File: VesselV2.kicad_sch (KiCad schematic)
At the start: 205 parts, among them U1 ATmega32U4-A

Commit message: Late night PCB organization (WIP)
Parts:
- added S1, S2, S3: MX_stab, PCM_marbastlib-mx:STAB_MX_P_2u, symbol PCM_marbastlib-mx:MX_stab
- added S4: MX_stab, PCM_marbastlib-mx:STAB_MX_P_6.25u, symbol PCM_marbastlib-mx:MX_stab
- MX45, MX61, MX91: footprint PCM_marbastlib-mx:STAB_MX_2u -> PCM_marbastlib-mx:SW_MX_1u
- MX97: footprint PCM_marbastlib-mx:STAB_MX_6.25u -> PCM_marbastlib-mx:SW_MX_1u
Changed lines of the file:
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@@
       (effects (font (size 1.27 1.27)))
     )
-    (property "Footprint" "PCM_marbastlib-mx:STAB_MX_6.25u" (at 196.85 162.56 0)
+    (property "Footprint" "PCM_marbastlib-mx:SW_MX_1u" (at 196.85 162.56 0)
       (effects (font (size 1.27 1.27)) hide)
     )
@@
     )
   )
+  (symbol (lib_id "PCM_marbastlib-mx:MX_stab") (at 194.31 203.2 0) (unit 1)
+    (in_bom yes) (on_board yes) (dnp no) (fields_autoplaced)
+    (property "Reference" "S4" (at 200.66 201.803 0)
+      (effects (font (size 1.27 1.27)) (justify left))
+    )
+    (property "Value" "MX_stab" (at 200.66 204.343 0)
+      (effects (font (size 1.27 1.27)) (justify left))
+    )
+    (property "Footprint" "PCM_marbastlib-mx:STAB_MX_P_6.25u" (at 194.31 203.2 0)
+      (effects (font (size 1.27 1.27)) hide)
+    )
+    (property "Datasheet" "" (at 194.31 203.2 0)
+      (effects (font (size 1.27 1.27)) hide)
+    )
+    (instances
+      (project "VesselV2"
+        (path "/c445c6d8-4fde-4143-815a-ac483f9e4cc3"
+          (reference "S4") (unit 1)
+        )
+      )
+    )
+  )
   (symbol (lib_id "PCM_marbastlib-mx:MX_SW_solder") (at 231.14 146.05 0) (unit 1)
     (in_bom yes) (on_board yes) (dnp no) (fields_autoplaced)
@@
       (effects (font (size 1.27 1.27)))
     )
-    (property "Footprint" "PCM_marbastlib-mx:STAB_MX_2u" (at 265.43 146.05 0)
+    (property "Footprint" "PCM_marbastlib-mx:SW_MX_1u" (at 265.43 146.05 0)
       (effects (font (size 1.27 1.27)) hide)
     )
@@
       (effects (font (size 1.27 1.27)))
     )
-    (property "Footprint" "PCM_marbastlib-mx:STAB_MX_2u" (at 276.86 111.76 0)
+    (property "Footprint" "PCM_marbastlib-mx:SW_MX_1u" (at 276.86 111.76 0)
       (effects (font (size 1.27 1.27)) hide)
     )
@@
     )
   )
+  (symbol (lib_id "PCM_marbastlib-mx:MX_stab") (at 311.15 177.8 0) (unit 1)
+    (in_bom yes) (on_board yes) (dnp no)
+    (property "Reference" "S1" (at 317.5 176.403 0)
+      (effects (font (size 1.27 1.27)) (justify left))
+    )
+    (property "Value" "MX_stab" (at 317.5 178.943 0)
+      (effects (font (size 1.27 1.27)) (justify left))
+    )
+    (property "Footprint" "PCM_marbastlib-mx:STAB_MX_P_2u" (at 311.15 177.8 0)
+      (effects (font (size 1.27 1.27)) hide)
+    )
+    (property "Datasheet" "" (at 311.15 177.8 0)
+      (effects (font (size 1.27 1.27)) hide)
+    )
+    (instances
+      (project "VesselV2"
+        (path "/c445c6d8-4fde-4143-815a-ac483f9e4cc3"
+          (reference "S1") (unit 1)
+        )
+      )
+    )
+  )
   (symbol (lib_id "Device:D_Small") (at 237.49 60.96 90) (unit 1)
     (in_bom yes) (on_board yes) (dnp no) (fields_autoplaced)
@@
     )
   )
+  (symbol (lib_id "PCM_marbastlib-mx:MX_stab") (at 309.88 189.23 0) (unit 1)
+    (in_bom yes) (on_board yes) (dnp no) (fields_autoplaced)
+    (property "Reference" "S2" (at 316.23 187.833 0)
+      (effects (font (size 1.27 1.27)) (justify left))
+    )
+    (property "Value" "MX_stab" (at 316.23 190.373 0)
+      (effects (font (size 1.27 1.27)) (justify left))
+    )
+    (property "Footprint" "PCM_marbastlib-mx:STAB_MX_P_2u" (at 309.88 189.23 0)
+      (effects (font (size 1.27 1.27)) hide)
+    )
+    (property "Datasheet" "" (at 309.88 189.23 0)
+      (effects (font (size 1.27 1.27)) hide)
+    )
+    (instances
+      (project "VesselV2"
+        (path "/c445c6d8-4fde-4143-815a-ac483f9e4cc3"
+          (reference "S2") (unit 1)
+        )
+      )
+    )
+  )
   (symbol (lib_id "PCM_marbastlib-mx:MX_SW_solder") (at 231.14 128.27 0) (unit 1)
     (in_bom yes) (on_board yes) (dnp no) (fields_autoplaced)
@@
       (effects (font (size 1.27 1.27)))
     )
-    (property "Footprint" "PCM_marbastlib-mx:STAB_MX_2u" (at 276.86 95.25 0)
+    (property "Footprint" "PCM_marbastlib-mx:SW_MX_1u" (at 276.86 95.25 0)
       (effects (font (size 1.27 1.27)) hide)
     )
@@
         )
       )
+    )
+  )
+  (symbol (lib_id "PCM_marbastlib-mx:MX_stab") (at 283.21 199.39 0) (unit 1)
+    (in_bom yes) (on_board yes) (dnp no) (fields_autoplaced)
+    (property "Reference" "S3" (at 289.56 197.993 0)
+      (effects (font (size 1.27 1.27)) (justify left))
+    )
+    (property "Value" "MX_stab" (at 289.56 200.533 0)
+      (effects (font (size 1.27 1.27)) (justify left))
+    )
+    (property "Footprint" "PCM_marbastlib-mx:STAB_MX_P_2u" (at 283.21 199.39 0)
+      (effects (font (size 1.27 1.27)) hide)
+    )
+    (property "Datasheet" "" (at 283.21 199.39 0)
+      (effects (font (size 1.27 1.27)) hide)
+    )
+    (instances
+      (project "VesselV2"
+        (path "/c445c6d8-4fde-4143-815a-ac483f9e4cc3"
+          (reference "S3") (unit 1)
+        )
+      )

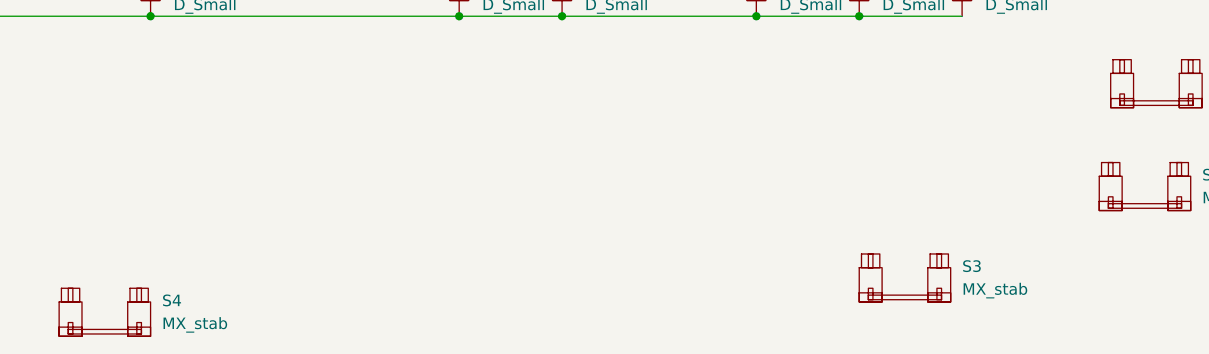
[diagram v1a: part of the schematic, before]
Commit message: Pcb build done - Adding crystal & labels
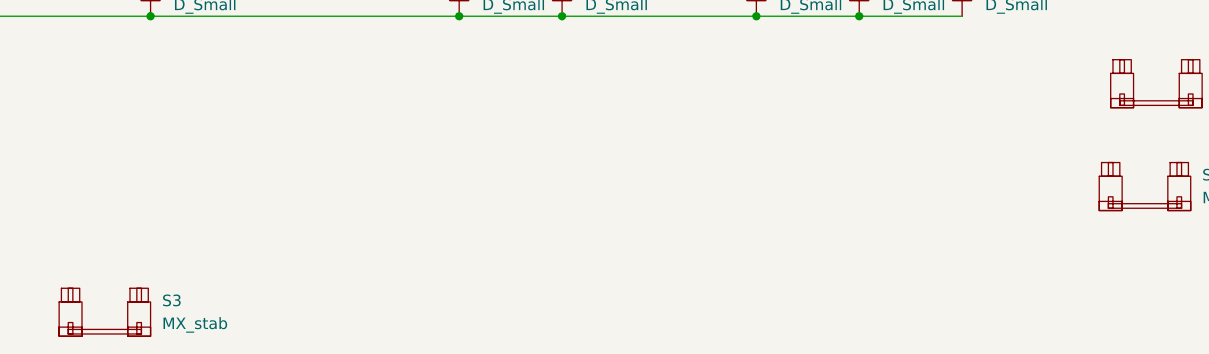
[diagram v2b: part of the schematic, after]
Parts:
- removed S3: MX_stab, PCM_marbastlib-mx:STAB_MX_P_2u, symbol PCM_marbastlib-mx:MX_stab
- MX91: footprint PCM_marbastlib-mx:SW_MX_1u -> PCM_marbastlib-mx:SW_MX_1.75u
- renumbered S4 to S3
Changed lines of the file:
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@@
   (symbol (lib_id "PCM_marbastlib-mx:MX_stab") (at 194.31 203.2 0) (unit 1)
     (in_bom yes) (on_board yes) (dnp no) (fields_autoplaced)
-    (property "Reference" "S4" (at 200.66 201.803 0)
+    (property "Reference" "S3" (at 200.66 201.803 0)
       (effects (font (size 1.27 1.27)) (justify left))
     )
@@
       (effects (font (size 1.27 1.27)) hide)
     )
+    (property "DigikeyPartNumber" "" (at 194.31 203.2 0)
+      (effects (font (size 1.27 1.27)))
+    )
     (instances
       (project "VesselV2"
         (path "/c445c6d8-4fde-4143-815a-ac483f9e4cc3"
-          (reference "S4") (unit 1)
+          (reference "S3") (unit 1)
         )
       )
@@
       (effects (font (size 1.27 1.27)))
     )
-    (property "Footprint" "PCM_marbastlib-mx:SW_MX_1u" (at 265.43 146.05 0)
+    (property "Footprint" "PCM_marbastlib-mx:SW_MX_1.75u" (at 265.43 146.05 0)
       (effects (font (size 1.27 1.27)) hide)
     )
@@
         )
       )
-    )
-  )
-  (symbol (lib_id "PCM_marbastlib-mx:MX_stab") (at 283.21 199.39 0) (unit 1)
-    (in_bom yes) (on_board yes) (dnp no) (fields_autoplaced)
-    (property "Reference" "S3" (at 289.56 197.993 0)
-      (effects (font (size 1.27 1.27)) (justify left))
-    )
-    (property "Value" "MX_stab" (at 289.56 200.533 0)
-      (effects (font (size 1.27 1.27)) (justify left))
-    )
-    (property "Footprint" "PCM_marbastlib-mx:STAB_MX_P_2u" (at 283.21 199.39 0)
-      (effects (font (size 1.27 1.27)) hide)
-    )
-    (property "Datasheet" "" (at 283.21 199.39 0)
-      (effects (font (size 1.27 1.27)) hide)
-    )
-    (instances
-      (project "VesselV2"
-        (path "/c445c6d8-4fde-4143-815a-ac483f9e4cc3"
-          (reference "S3") (unit 1)
-        )
-      )

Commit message: Footprint Assignment
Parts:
- added C1, C3: 22pF, Capacitor_SMD:C_0805_2012Metric_Pad1.18x1.45mm_HandSolder, symbol Device:C_Small
- added C2: 1uf, Capacitor_SMD:C_0805_2012Metric_Pad1.18x1.45mm_HandSolder, symbol Device:C_Small
- added F1: 500mA, Fuse:Fuse_1206_3216Metric_Pad1.42x1.75mm_HandSolder, symbol Device:Polyfuse_Small
- added J1: USB_A, Connector_USB:USB_A_Molex_67643_Horizontal, symbol Connector:USB_A
- added R2, R3: 22, Resistor_SMD:R_0805_2012Metric_Pad1.20x1.40mm_HandSolder, symbol Device:R_Small
- added R4, R5: 10k, Resistor_SMD:R_0805_2012Metric_Pad1.20x1.40mm_HandSolder, symbol Device:R_Small
- added SW1: SW_Push, symbol Switch:SW_Push
- added Y1: 16MHz, Crystal:Crystal_SMD_3225-4Pin_3.2x2.5mm_HandSoldering, symbol Device:Crystal_GND24_Small
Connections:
- net ROW6: now reaches D100.1 (K), D101.1 (K), D102.1 (K), D94.1 (K), D95.1 (K), D96.1 (K), D97.1 (K), D98.1 (K), D99.1 (K)
- net ROW6: now also U1.20 (PD2)
- net ROW2: now reaches U1.10 (PB2)
- net ROW2: now also D32.1 (K), D33.1 (K), D34.1 (K), D35.1 (K), D36.1 (K), D37.1 (K), D38.1 (K), D39.1 (K), D40.1 (K), D41.1 (K), D42.1 (K), D43.1 (K), D44.1 (K), D45.1 (K), D46.1 (K), D47.1 (K)
- net ROW3: now reaches U1.11 (PB3)
- net ROW3: now also D48.1 (K), D49.1 (K), D50.1 (K), D51.1 (K), D52.1 (K), D53.1 (K), D54.1 (K), D55.1 (K), D56.1 (K), D57.1 (K), D58.1 (K), D59.1 (K), D60.1 (K), D61.1 (K), D62.1 (K), D63.1 (K)
- net COL0: now reaches U1.12 (PB7)
- net COL0: now also MX1.1, MX16.1, MX32.1, MX48.1, MX64.1, MX79.1, MX94.1
- net at U1.13 (~{RESET}): now also R4.1, SW1.2
- net +5V: now reaches U1.14 (VCC), U1.34 (VCC)
- net +5V: now also U1.2 (UVCC), U1.24 (AVCC), U1.44 (AVCC), U1.7 (VBUS), F1.2, R4.2
- net GND: now reaches U1.15 (GND), U1.23 (GND), U1.35 (GND), U1.43 (GND)
- net GND: now also U1.5 (UGND), C1.1, C2.2, C3.1, J1.4 (GND), R5.2, SW1.1, Y1.2, Y1.4
- net at U1.16 (XTAL2): now also C3.2, Y1.3
- net at U1.17 (XTAL1): now also C1.2, Y1.1
- net ROW4: now reaches U1.18 (PD0)
- net ROW4: now also D64.1 (K), D65.1 (K), D66.1 (K), D67.1 (K), D68.1 (K), D69.1 (K), D70.1 (K), D71.1 (K), D72.1 (K), D73.1 (K), D74.1 (K), D75.1 (K), D76.1 (K), D77.1 (K), D78.1 (K)
- net ROW5: now reaches U1.19 (PD1)
- net ROW5: now also D79.1 (K), D80.1 (K), D81.1 (K), D82.1 (K), D83.1 (K), D84.1 (K), D85.1 (K), D86.1 (K), D87.1 (K), D88.1 (K), D89.1 (K), D90.1 (K), D91.1 (K), D92.1 (K), D93.1 (K)
- net COL1: now reaches U1.21 (PD3)
- net COL1: now also MX2.1, MX33.1, MX49.1, MX65.1, MX80.1, MX95.1
- net COL2: now reaches U1.22 (PD5)
- net COL2: now also MX17.1, MX3.1, MX34.1, MX50.1, MX66.1, MX81.1, MX96.1
- net COL3: now reaches U1.25 (PD4)
- net COL3: now also MX18.1, MX35.1, MX4.1, MX51.1, MX67.1, MX82.1
- net COL4: now reaches U1.26 (PD6)
- net COL4: now also MX19.1, MX36.1, MX5.1, MX52.1, MX68.1, MX83.1
- net COL5: now reaches U1.27 (PD7)
- net COL5: now also MX20.1, MX37.1, MX53.1, MX6.1, MX69.1, MX84.1
- net COL6: now reaches U1.28 (PB4)
- net COL6: now also MX21.1, MX38.1, MX54.1, MX7.1, MX70.1, MX85.1, MX97.1
- net COL7: now reaches U1.29 (PB5)
- net COL7: now also MX22.1, MX39.1, MX55.1, MX71.1, MX8.1, MX86.1
- net at U1.3 (D-): now also R3.2
- net COL8: now reaches U1.30 (PB6)
- net COL8: now also MX24.1, MX41.1, MX57.1, MX73.1, MX88.1, MX98.1
- net COL9: now reaches U1.31 (PC6)
- net COL9: now also MX23.1, MX40.1, MX56.1, MX72.1, MX87.1, MX9.1
- net COL10: now reaches U1.32 (PC7)
- net COL10: now also MX10.1, MX25.1, MX42.1, MX58.1, MX74.1, MX89.1, MX99.1
- net at U1.33 (~{HWB}/PE2): now also R5.1
- net COL11: now reaches U1.36 (PF7)
- net COL11: now also MX11.1, MX26.1, MX43.1, MX59.1, MX75.1, MX90.1
- net COL12: now reaches U1.37 (PF6)
- net COL12: now also MX100.1, MX12.1, MX27.1, MX44.1, MX60.1, MX76.1, MX91.1
- net COL13: now reaches U1.38 (PF5)
- net COL13: now also MX101.1, MX28.1, MX45.1, MX61.1, MX92.1
- net COL14: now reaches U1.39 (PF4)
- net COL14: now also MX102.1, MX13.1, MX29.1
- net at U1.4 (D+): now also R2.2
- net COL15: now reaches U1.40 (PF1)
- net COL15: now also MX14.1, MX30.1, MX46.1, MX62.1, MX77.1
- net COL16: now reaches U1.41 (PF0)
- net COL16: now also MX15.1, MX31.1, MX47.1, MX63.1, MX78.1, MX93.1
- net at U1.6 (UCAP): now also C2.1
- net ROW0: now reaches U1.8 (PB0)
- net ROW0: now also D1.1 (K), D10.1 (K), D11.1 (K), D12.1 (K), D13.1 (K), D14.1 (K), D15.1 (K), D2.1 (K), D3.1 (K), D4.1 (K), D5.1 (K), D6.1 (K), D7.1 (K), D8.1 (K), D9.1 (K)
- net ROW1: now reaches U1.9 (PB1)
- net ROW1: now also D16.1 (K), D17.1 (K), D18.1 (K), D19.1 (K), D20.1 (K), D21.1 (K), D22.1 (K), D23.1 (K), D24.1 (K), D25.1 (K), D26.1 (K), D27.1 (K), D28.1 (K), D29.1 (K), D30.1 (K), D31.1 (K)
- new net D+: J1.3 (D+), R2.1
- new net D-: J1.2 (D-), R3.1
- new net VCC: F1.1, J1.1 (VBUS)
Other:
- moved on the sheet: D1, D10, D100, D101, D102, D11, D12, D13, D14, D15, D16, D17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

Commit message: Footprint Assignment & Part Number association
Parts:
- removed J1: USB_A, Connector_USB:USB_A_Molex_67643_Horizontal, symbol Connector:USB_A
- added USB1: Molex-0548190589, random-keyboard-parts:Molex-0548190589, symbol random-keyboard-parts:Molex-0548190589
- C1, C3: DigikeyPartNumber (none) -> 311-1103-6-ND
- F1: DigikeyPartNumber (none) -> 486-1675-6-ND
- R2, R3: DigikeyPartNumber (none) -> RMCF0805FT22R0DKR-ND
- R4, R5: DigikeyPartNumber (none) -> RMCF0805FT10K0DKR-ND
- SW1: footprint (none) -> random-keyboard-parts:SKQG-1155865; ManufacturerPartNumber (none) -> SKQGACE010
- U1: DigikeyPartNumber (none) -> ATMEGA32U4-AU-ND
- Y1: DigikeyPartNumber (none) -> SER4069DKR-ND
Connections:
- net D+: now also USB1.3 (D+)
- net D-: now also USB1.4 (D-)
- net GND: now also USB1.1 (GND), USB1.6 (SHIELD)
- net VCC: now also USB1.5 (VBUS)
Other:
- moved on the sheet: F1

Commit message: Edge cuts done - Datasheet info filled in - Preliminary Bom generated
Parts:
- C2: DigikeyPartNumber (none) -> 399-C0402C105K9PAC7867DKR-ND
- D1, D10, D100, D101, D102, D11, D12, D13, D14, D15, D16, D17, D18, D19, D2, D20, D21, D22, D23, D24, D25, D26, D27, D28, D29, D3, D30, D31, D32, D33, D34, D35, D36, D37, D38, D39, D4, D40, D41, D42, D43, D44, D45, D46, D47, D48, D49, D5, D50, D51, D52, D53, D54, D55, D56, D57, D58, D59, D6, D60, D61, D62, D63, D64, D65, D66, D67, D68, D69, D7, D70, D71, D72, D73, D74, D75, D76, D77, D78, D79, D8, D80, D81, D82, D83, D84, D85, D86, D87, D88, D89, D9, D90, D91, D92, D93, D94, D95, D96, D97, D98, D99: DigikeyPartNumber (none) -> 1N4148WTPMSDKR-ND; ManufacturerPartNumber (none) -> 1N4148W
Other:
- moved on the sheet: R4

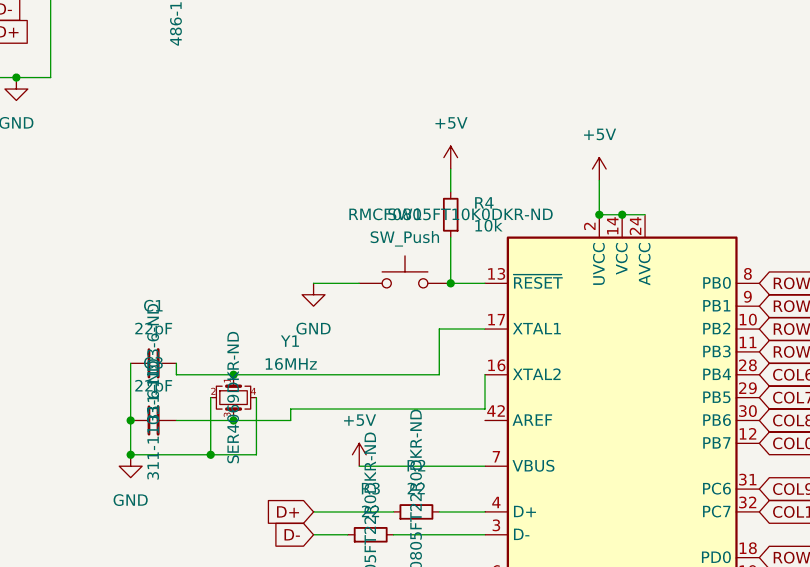
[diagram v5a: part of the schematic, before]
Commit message: Mouser partNumber fields Update - BOM Update
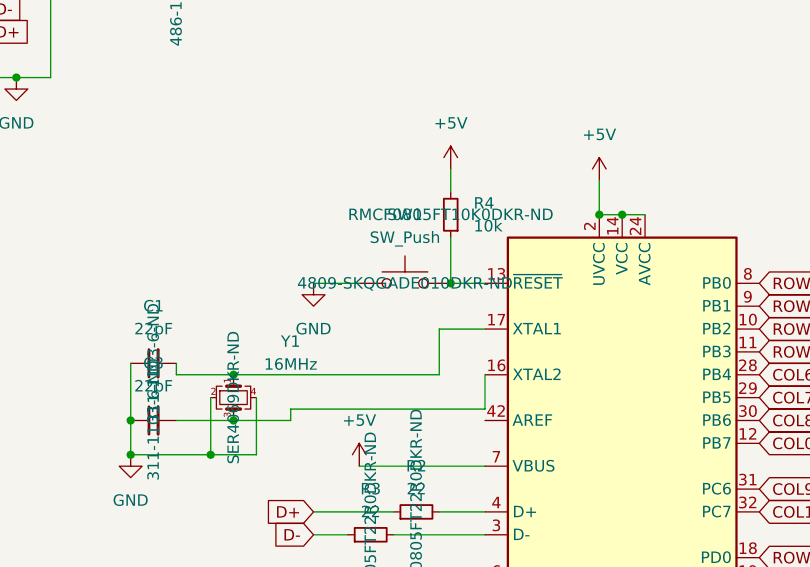
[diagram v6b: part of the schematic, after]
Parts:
- C1, C3: MouserPartNumber (none) -> 603-CC805JRNPO9BN220
- C2: MouserPartNumber (none) -> 80-C0402C105K9P
- D1, D10, D100, D101, D102, D11, D12, D13, D14, D15, D16, D17, D18, D19, D2, D20, D21, D22, D23, D24, D25, D26, D27, D28, D29, D3, D30, D31, D32, D33, D34, D35, D36, D37, D38, D39, D4, D40, D41, D42, D43, D44, D45, D46, D47, D48, D49, D5, D50, D51, D52, D53, D54, D55, D56, D57, D58, D59, D6, D60, D61, D62, D63, D64, D65, D66, D67, D68, D69, D7, D70, D71, D72, D73, D74, D75, D76, D77, D78, D79, D8, D80, D81, D82, D83, D84, D85, D86, D87, D88, D89, D9, D90, D91, D92, D93, D94, D95, D96, D97, D98, D99: MouserPartNumber (none) -> 833-1N4148W-TP
- F1: MouserPartNumber (none) -> 693-3413.0113.22
- R2, R3: MouserPartNumber (none) -> 708-RMCF0805FT22R0
- R4, R5: MouserPartNumber (none) -> 708-RMCF0805FT10K0
- SW1: DigikeyPartNumber (none) -> 4809-SKQGADE010DKR-ND; MouserPartNumber (none) -> 688-SKQGAD
- U1: MouserPartNumber (none) -> 556-ATMEGA32U4-AU
- USB1: MouserPartNumber (none) -> 538-54819-0589
- Y1: MouserPartNumber (none) -> 732-322516MF09Z-AC0

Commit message: Fixed routing errors - except USB footprint shape
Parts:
- S2: footprint PCM_marbastlib-mx:STAB_MX_P_2u -> PCM_marbastlib-mx:STAB_MX_P_ISO
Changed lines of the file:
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@@
       (effects (font (size 1.27 1.27)) (justify left))
     )
-    (property "Footprint" "PCM_marbastlib-mx:STAB_MX_P_2u" (at 250.19 236.22 0)
+    (property "Footprint" "PCM_marbastlib-mx:STAB_MX_P_ISO" (at 250.19 236.22 0)
       (effects (font (size 1.27 1.27)) hide)
     )
